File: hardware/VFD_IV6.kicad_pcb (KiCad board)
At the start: 4 copper layers, 110 x 54 mm, 127 parts, among them J1 USB_C, J2 SWD, J3 Power, J4 Conn_01x10, J5 Conn_01x06, Q1 BC817, Q2 BC817, SW1 RotaryEncoder_Switch_MP, SW2 MODE, U1 LP2985-3.3, U10 4511, U11 4511, U12 4511, U13 4511, U14 TBD62783A, U15 TBD62783A, U16 TBD62783A, U17 TBD62783A, U18 TBD62783A, U19 TBD62783A, U2 MP2307, U3 LM2733XMF, U4 DS1302Z+, U5 STM32F103C8T6, U6 74HC04, U7 4017, U8 4511, U9 4511, Y1 32.768 KHz, Y2 8MHz

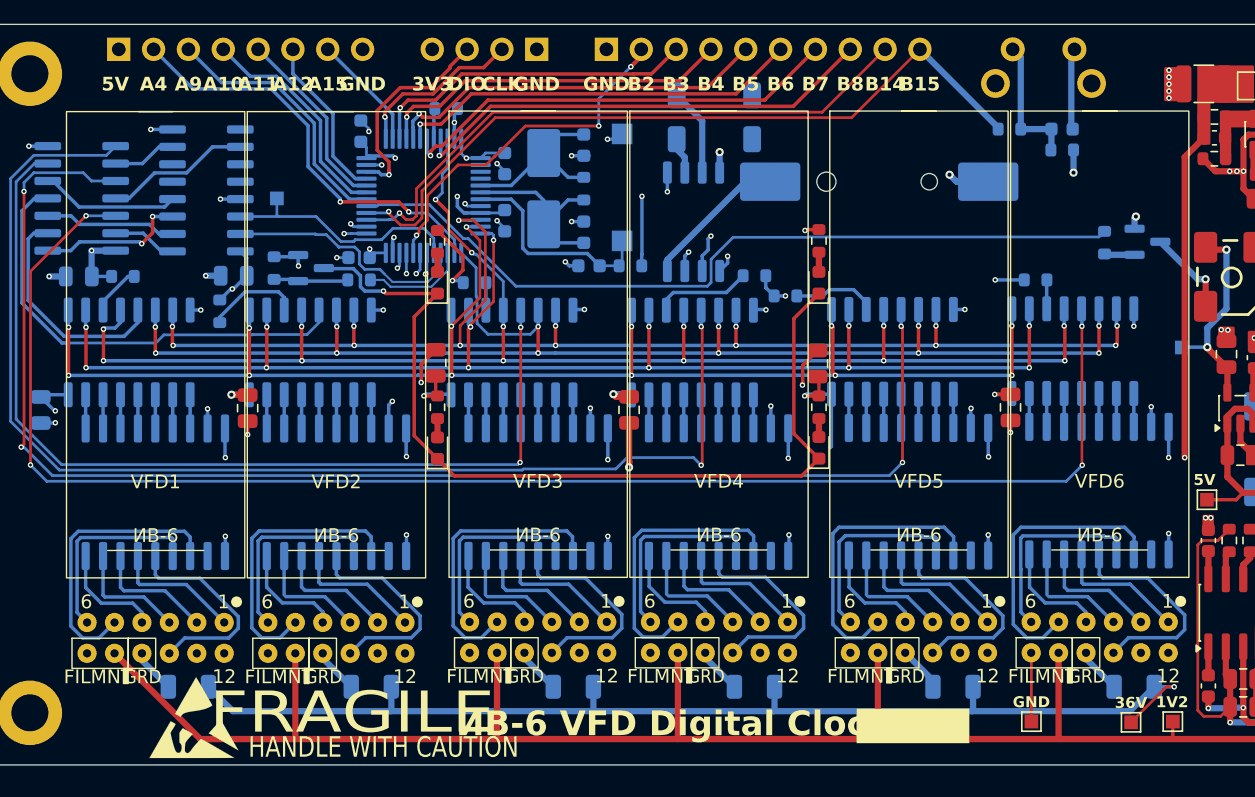
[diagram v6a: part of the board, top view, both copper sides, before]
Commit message: Replaced the RTC chip with PCF8563T
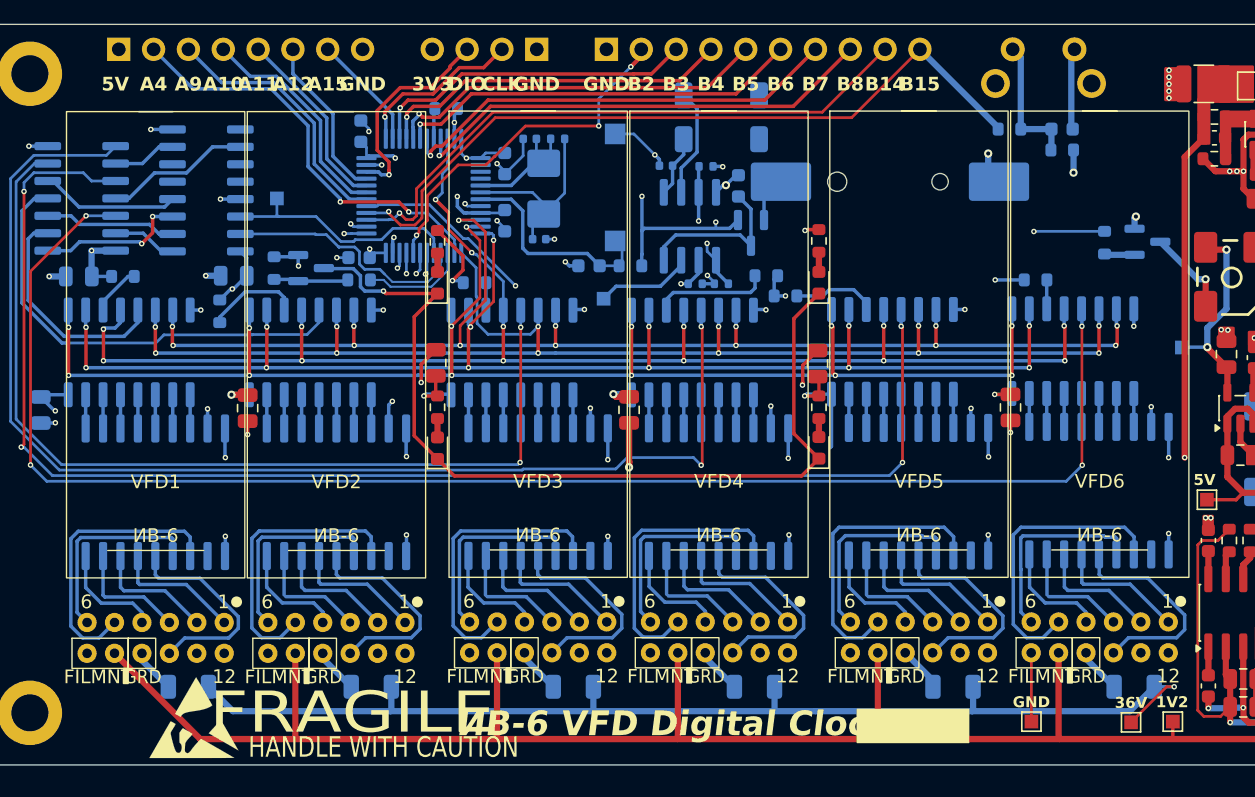
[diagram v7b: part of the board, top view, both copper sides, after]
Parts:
- removed U4: DS1302Z+, Package_SO:SOIC-8_5.3x5.3mm_P1.27mm
- added C33: 100n, Capacitor_SMD:C_0603_1608Metric, B.Cu at (113.8, 68.4)
- added C34: 22p, Capacitor_SMD:C_0402_1005Metric, B.Cu at (108.5, 66.9)
- added D7: BAV70, Package_TO_SOT_SMD:SOT-23, B.Cu at (114.7, 71.8)
- added R37: 4k7, Resistor_SMD:R_0402_1005Metric, B.Cu at (110.6, 75.5)
- added R38: 4k7, Resistor_SMD:R_0402_1005Metric, B.Cu at (112.5, 75.5)
- added R39: 4k7, Resistor_SMD:R_0402_1005Metric, B.Cu at (111.4, 67.0)
- added TP5: CLKO, TestPoint:TestPoint_Pad_1.0x1.0mm, B.Cu at (103.9, 76.6)
- added U20: PCF8563T, Package_SO:SOIC-8_3.9x4.9mm_P1.27mm, B.Cu at (110.2, 71.3)
- C17, C18: footprint Capacitor_SMD:C_0603_1608Metric -> Capacitor_SMD:C_0402_1005Metric
- R20: footprint Resistor_SMD:R_0603_1608Metric -> Resistor_SMD:R_0402_1005Metric
- Y2: footprint Crystal:Crystal_SMD_5032-2Pin_5.0x3.2mm_HandSoldering -> Crystal:Crystal_SMD_5032-2Pin_5.0x3.2mm
- moved R20 4.10 mm to (100.6, 64.9), turned to 0 degrees
- moved C17 3.96 mm to (98.6, 64.9), turned to 0 degrees
- moved C18 3.29 mm to (99.2, 72.3), turned to 180 degrees
- moved R28 0.86 mm to (115.8, 74.9)
- moved BT1 0.79 mm to (124.9, 68.1)
- moved Y1 0.51 mm to (112.5, 63.4)
- moved RESET1 0.51 mm to (104.8, 68.5)
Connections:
- U5 pad 18: /RTC_RES -> /RTC_INT
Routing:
- net /RTC_INT: track 0.00 -> 27.2 mm, vias 0 -> 2
- net /RTC_RES: track 26.3 -> 0.00 mm, vias 2 -> 0
- net +3V3: track 148.8 -> 163.7 mm, vias 10 -> 12
- net Net-(D7-K): track 0.00 -> 12.0 mm
- net Net-(BT1-+): track 10.7 -> 3.31 mm
- net Net-(U20-CLKO): track 0.00 -> 7.04 mm
- net GND: track 106.1 -> 111.5 mm, vias 74 -> 73
- net /OSC_OUT: track 12.0 -> 14.0 mm
- net Net-(U20-OSCI): track 2.68 -> 4.48 mm
- net Net-(U20-OSCO): track 6.40 -> 7.96 mm
- net /OSC_IN: track 11.0 -> 9.58 mm
- net Net-(U11-~{LT}): track 7.05 -> 8.44 mm
- net /RTC_DAT: track 27.1 -> 28.1 mm
- net /BUZZER: track 59.0 -> 58.8 mm, vias 0 -> 2
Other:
- board text added: "RESET"
- board text added: "RTCOSC"
- board text added: "ВЕРНИ НА"
- board text added: "МЕСТО!"
- board text removed: "RST"
